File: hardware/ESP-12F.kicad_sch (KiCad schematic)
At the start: 37 parts, among them J10 PROG_PORT, U10 ESP-12F, U11 MCP2558FD-xMF, U8 PI4IOE5V6416LEX, U9 PI4IOE5V6416LEX

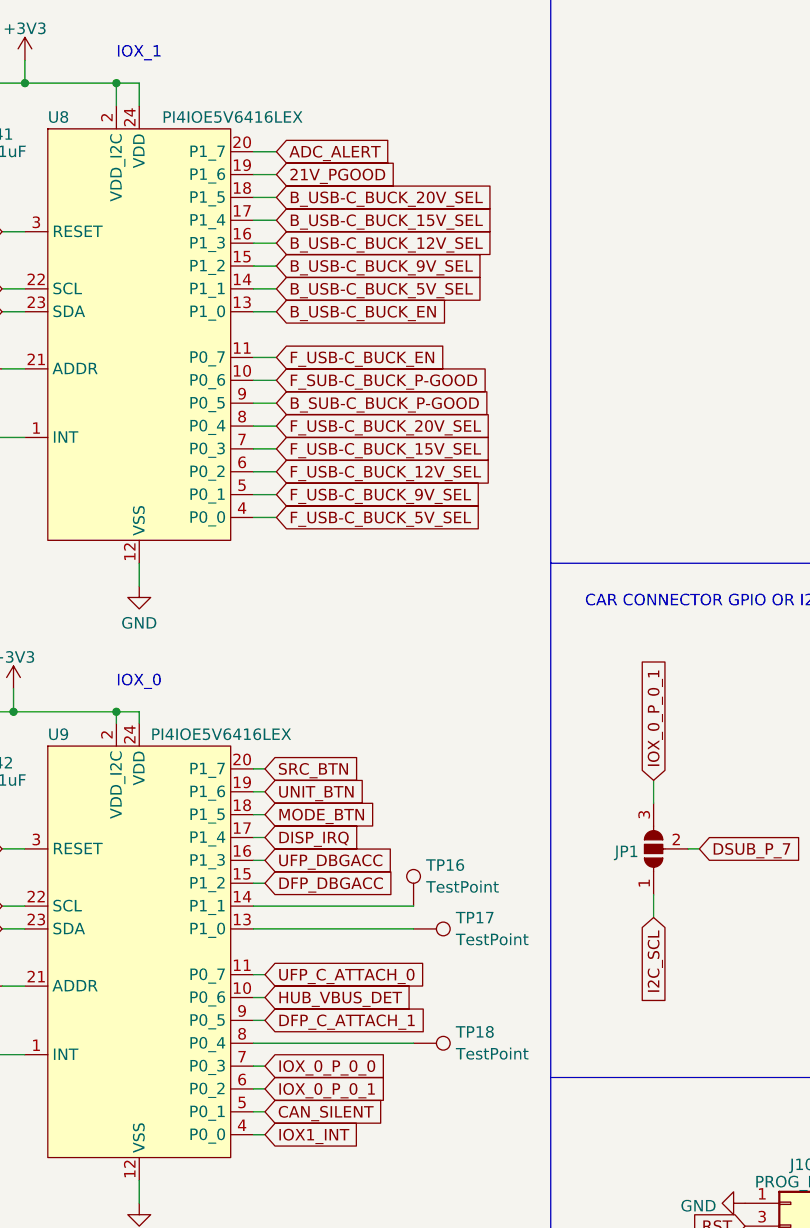
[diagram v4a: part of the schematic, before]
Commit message: switched pd phy as old one needed an NDA
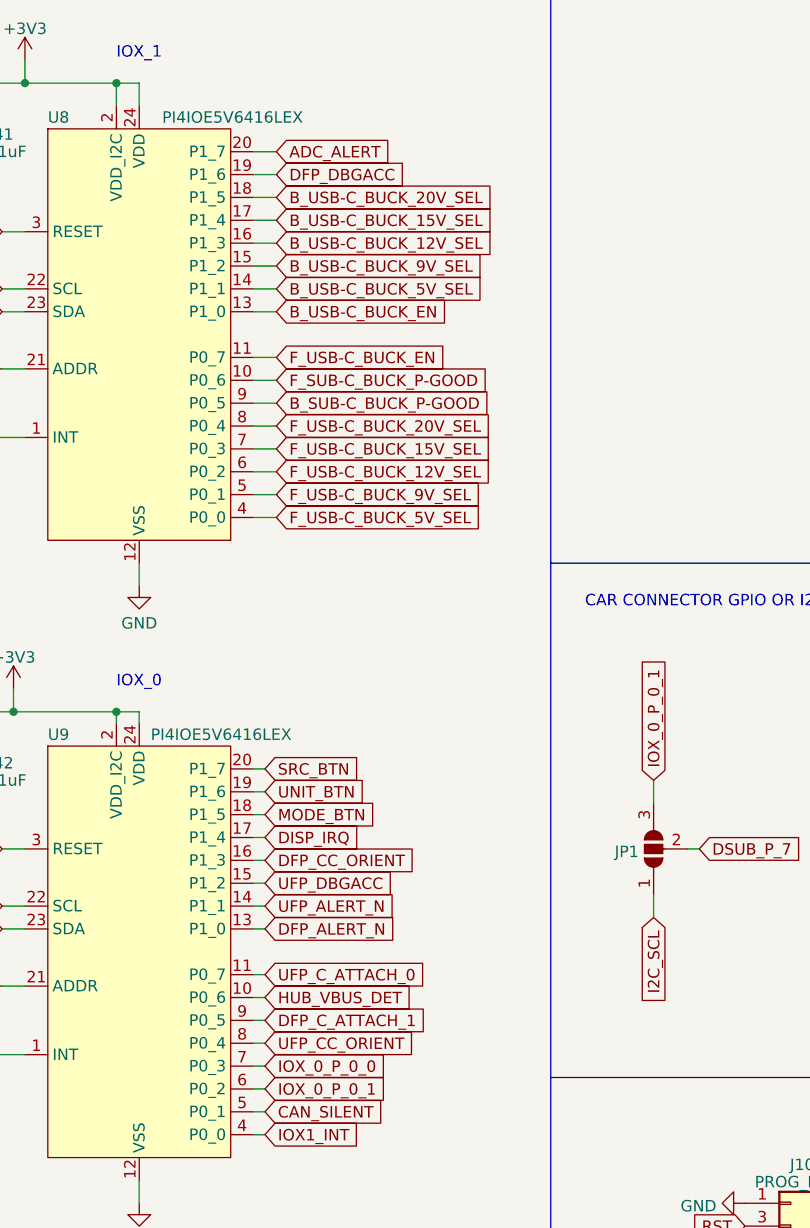
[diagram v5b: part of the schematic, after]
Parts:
- removed TP16, TP17, TP18: TestPoint, TestPoint:TestPoint_Pad_D1.5mm, symbol Connector:TestPoint
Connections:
- net 21V_PGOOD is gone; now on net DFP_DBGACC: U8.19 (P1_6)
- net DFP_DBGACC: no longer U9.15 (P1_2)
- net UFP_DBGACC: now also U9.15 (P1_2); no longer U9.16 (P1_3)
- net DFP_ALERT_N: now reaches U9.13 (P1_0)
- net UFP_ALERT_N: now reaches U9.14 (P1_1)
- net UFP_CC_ORIENT: now reaches U9.8 (P0_4)
- new net DFP_CC_ORIENT: U9.16 (P1_3)
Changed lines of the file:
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@@
-    (stroke (width 0) (type default))
-  )
-  (wire (pts (xy 82.55 149.86) (xy 100.33 149.86))
     (stroke (width 0) (type default))
   )
@@
     (stroke (width 0) (type default))
   )
+  (wire (pts (xy 82.55 149.86) (xy 83.82 149.86))
+    (stroke (width 0) (type default))
+  )
   (wire (pts (xy 217.17 130.81) (xy 219.71 130.81))
     (stroke (width 0) (type default))
@@
     (stroke (width 0) (type default))
   )
-  (wire (pts (xy 82.55 137.16) (xy 100.33 137.16))
-    (stroke (width 0) (type default))
-  )
   (wire (pts (xy 82.55 124.46) (xy 83.82 124.46))
     (stroke (width 0) (type default))
@@
     (stroke (width 0) (type default))
   )
+  (wire (pts (xy 82.55 137.16) (xy 83.82 137.16))
+    (stroke (width 0) (type default))
+  )
   (wire (pts (xy 153.67 133.35) (xy 153.67 135.89))
     (stroke (width 0) (type default))
@@
     (stroke (width 0) (type default))
   )
+  (wire (pts (xy 82.55 134.62) (xy 83.82 134.62))
+    (stroke (width 0) (type default))
+  )
   (wire (pts (xy 49.53 43.18) (xy 49.53 45.72))
     (stroke (width 0) (type default))
@@
   )
   (wire (pts (xy 201.93 87.63) (xy 201.93 83.82))
-    (stroke (width 0) (type default))
-  )
-  (wire (pts (xy 82.55 134.62) (xy 100.33 134.62))
     (stroke (width 0) (type default))
   )
@@
     )
   )
+  (global_label "UFP_CC_ORIENT" (shape input) (at 83.82 149.86 0) (fields_autoplaced)
+    (effects (font (size 1.27 1.27)) (justify left))
+    (property "Intersheetrefs" "${INTERSHEET_REFS}" (at 101.6219 149.86 0)
+      (effects (font (size 1.27 1.27)) (justify left) hide)
+    )
+  )
   (global_label "F_USB-C_BUCK_5V_SEL" (shape input) (at 85.09 91.44 0) (fields_autoplaced)
     (effects (font (size 1.27 1.27)) (justify left))
@@
     (effects (font (size 1.27 1.27)) (justify left))
     (property "Intersheetrefs" "${INTERSHEET_REFS}" (at 111.8233 81.28 0)
-      (effects (font (size 1.27 1.27)) (justify left) hide)
-    )
-  )
-  (global_label "21V_PGOOD" (shape input) (at 85.09 53.34 0) (fields_autoplaced)
-    (effects (font (size 1.27 1.27)) (justify left))
-    (property "Intersheetrefs" "${INTERSHEET_REFS}" (at 98.942 53.34 0)
       (effects (font (size 1.27 1.27)) (justify left) hide)
     )
@@
     )
   )
+  (global_label "UFP_ALERT_N" (shape input) (at 83.82 134.62 0) (fields_autoplaced)
+    (effects (font (size 1.27 1.27)) (justify left))
+    (property "Intersheetrefs" "${INTERSHEET_REFS}" (at 99.2633 134.62 0)
+      (effects (font (size 1.27 1.27)) (justify left) hide)
+    )
+  )
   (global_label "I2C_SDA" (shape input) (at 261.62 60.96 90) (fields_autoplaced)
     (effects (font (size 1.27 1.27)) (justify left))
@@
     )
   )
-  (global_label "UFP_DBGACC" (shape input) (at 83.82 129.54 0) (fields_autoplaced)
-    (effects (font (size 1.27 1.27)) (justify left))
-    (property "Intersheetrefs" "${INTERSHEET_REFS}" (at 98.8211 129.54 0)
+  (global_label "DFP_ALERT_N" (shape input) (at 83.82 137.16 0) (fields_autoplaced)
+    (effects (font (size 1.27 1.27)) (justify left))
+    (property "Intersheetrefs" "${INTERSHEET_REFS}" (at 99.2028 137.16 0)
+      (effects (font (size 1.27 1.27)) (justify left) hide)
+    )
+  )
+  (global_label "UFP_DBGACC" (shape input) (at 83.82 132.08 0) (fields_autoplaced)
+    (effects (font (size 1.27 1.27)) (justify left))
+    (property "Intersheetrefs" "${INTERSHEET_REFS}" (at 98.8211 132.08 0)
       (effects (font (size 1.27 1.27)) (justify left) hide)
     )
@@
     )
   )
-  (global_label "DFP_DBGACC" (shape input) (at 83.82 132.08 0) (fields_autoplaced)
-    (effects (font (size 1.27 1.27)) (justify left))
-    (property "Intersheetrefs" "${INTERSHEET_REFS}" (at 98.7606 132.08 0)
+  (global_label "DFP_DBGACC" (shape input) (at 85.09 53.34 0) (fields_autoplaced)
+    (effects (font (size 1.27 1.27)) (justify left))
+    (property "Intersheetrefs" "${INTERSHEET_REFS}" (at 100.0306 53.34 0)
       (effects (font (size 1.27 1.27)) (justify left) hide)
     )
@@
     (effects (font (size 1.27 1.27)) (justify left))
     (property "Intersheetrefs" "${INTERSHEET_REFS}" (at 106.441 73.66 0)
+      (effects (font (size 1.27 1.27)) (justify left) hide)
+    )
+  )
+  (global_label "DFP_CC_ORIENT" (shape input) (at 83.82 129.54 0) (fields_autoplaced)
+    (effects (font (size 1.27 1.27)) (justify left))
+    (property "Intersheetrefs" "${INTERSHEET_REFS}" (at 101.5614 129.54 0)
       (effects (font (size 1.27 1.27)) (justify left) hide)
     )
@@
         (path "/fae025e9-99c5-40c1-af6f-99dc1edbfa43/62352716-6578-44e5-ac45-fc6ae860b12d"
           (reference "#PWR049") (unit 1)
-        )
-      )
-    )
-  )
-  (symbol (lib_id "Connector:TestPoint") (at 100.33 137.16 270) (unit 1)
-    (in_bom yes) (on_board yes) (dnp no) (fields_autoplaced)
-    (property "Reference" "TP17" (at 105.029 135.9479 90)
-      (effects (font (size 1.27 1.27)) (justify left))
-    )
-    (property "Value" "TestPoint" (at 105.029 138.3721 90)
-      (effects (font (size 1.27 1.27)) (justify left))
-    )
-    (property "Footprint" "TestPoint:TestPoint_Pad_D1.5mm" (at 100.33 142.24 0)
-      (effects (font (size 1.27 1.27)) hide)
-    )
-    (property "Datasheet" "~" (at 100.33 142.24 0)
-      (effects (font (size 1.27 1.27)) hide)
-    )
-    (pin "1")
-    (instances
-      (project "usbc-car-module"
-        (path "/fae025e9-99c5-40c1-af6f-99dc1edbfa43/62352716-6578-44e5-ac45-fc6ae860b12d"
-          (reference "TP17") (unit 1)
         )
       )
@@
         )
       )
-    )
-  )
-  (symbol (lib_id "Connector:TestPoint") (at 100.33 149.86 270) (unit 1)
-    (in_bom yes) (on_board yes) (dnp no) (fields_autoplaced)
-    (property "Reference" "TP18" (at 105.029 148.6479 90)
-      (effects (font (size 1.27 1.27)) (justify left))
-    )
-    (property "Value" "TestPoint" (at 105.029 151.0721 90)
-      (effects (font (size 1.27 1.27)) (justify left))
-    )
-    (property "Footprint" "TestPoint:TestPoint_Pad_D1.5mm" (at 100.33 154.94 0)
-      (effects (font (size 1.27 1.27)) hide)
-    )
-    (property "Datasheet" "~" (at 100.33 154.94 0)
-      (effects (font (size 1.27 1.27)) hide)
-    )
-    (pin "1")
-    (instances
-      (project "usbc-car-module"
-        (path "/fae025e9-99c5-40c1-af6f-99dc1edbfa43/62352716-6578-44e5-ac45-fc6ae860b12d"
-          (reference "TP18") (unit 1)
-        )
-      )
-    )
-  )
-  (symbol (lib_id "Connector:TestPoint") (at 100.33 134.62 0) (unit 1)
-    (in_bom yes) (on_board yes) (dnp no) (fields_autoplaced)
-    (property "Reference" "TP16" (at 101.727 130.1059 0)
-      (effects (font (size 1.27 1.27)) (justify left))
-    )
-    (property "Value" "TestPoint" (at 101.727 132.5301 0)
-      (effects (font (size 1.27 1.27)) (justify left))
-    )
-    (property "Footprint" "TestPoint:TestPoint_Pad_D1.5mm" (at 105.41 134.62 0)
-      (effects (font (size 1.27 1.27)) hide)
-    )
-    (property "Datasheet" "~" (at 105.41 134.62 0)
-      (effects (font (size 1.27 1.27)) hide)
-    )
-    (pin "1")
-    (instances
-      (project "usbc-car-module"
-        (path "/fae025e9-99c5-40c1-af6f-99dc1edbfa43/62352716-6578-44e5-ac45-fc6ae860b12d"
-          (reference "TP16") (unit 1)
-        )
-      )

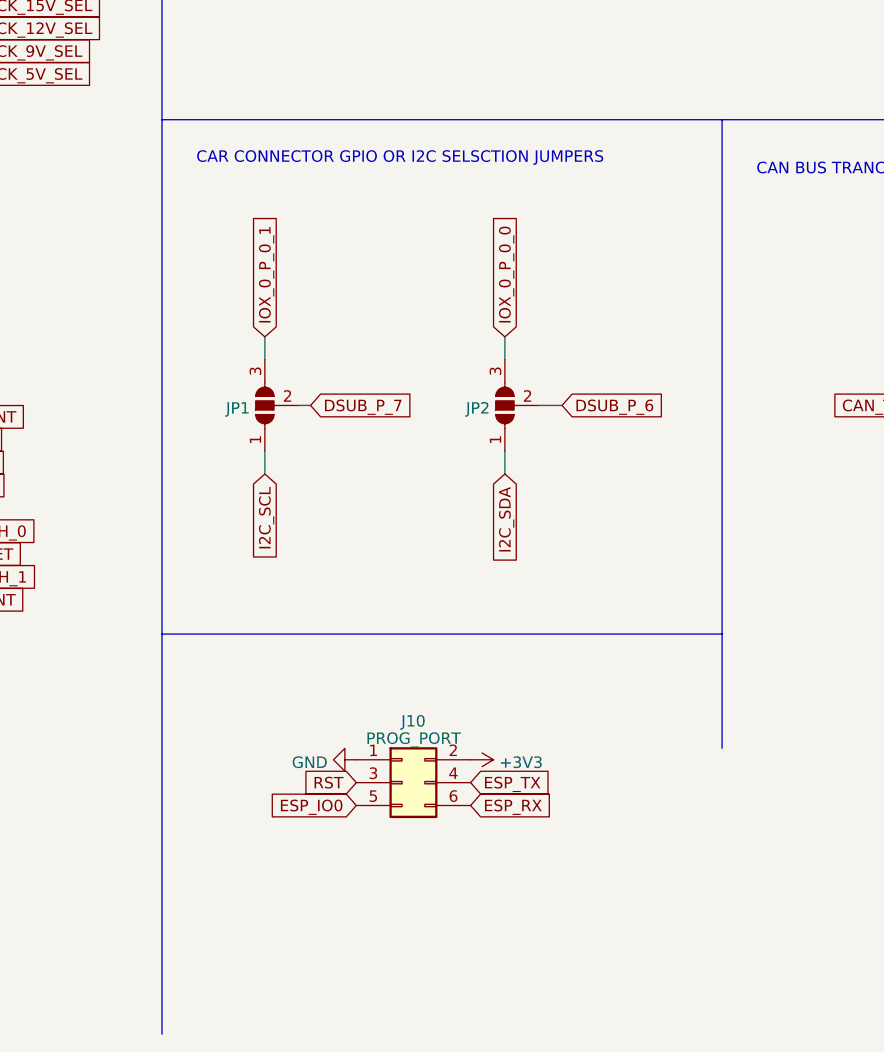
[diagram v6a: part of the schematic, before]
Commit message: added eeprom for nonvol memory
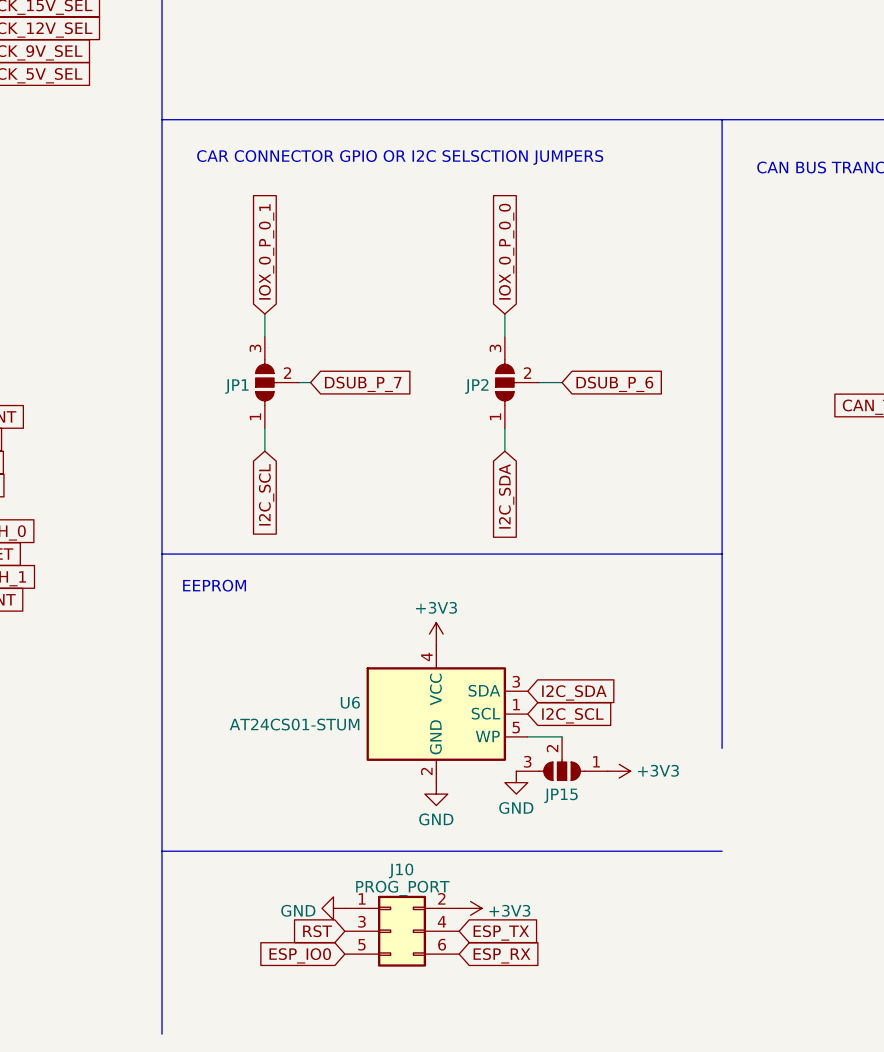
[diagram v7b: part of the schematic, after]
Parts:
- added JP15: ~, Jumper:SolderJumper-3_P1.3mm_Open_RoundedPad1.0x1.5mm_NumberLabels, symbol Jumper:SolderJumper_3_Open
- added U6: AT24CS01-STUM, Package_TO_SOT_SMD:SOT-23-5, symbol Memory_EEPROM:AT24CS01-STUM
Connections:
- net +3V3: now also JP15.1 (A), U6.4 (VCC)
- net GND: now also JP15.3 (B), U6.2 (GND)
- net I2C_SCL: now also U6.1 (SCL)
- net I2C_SDA: now also U6.3 (SDA)
- new net: JP15.2 (C), U6.5 (WP)
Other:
- note added: "EEPROM"
- moved on the sheet: J10, JP1, JP2

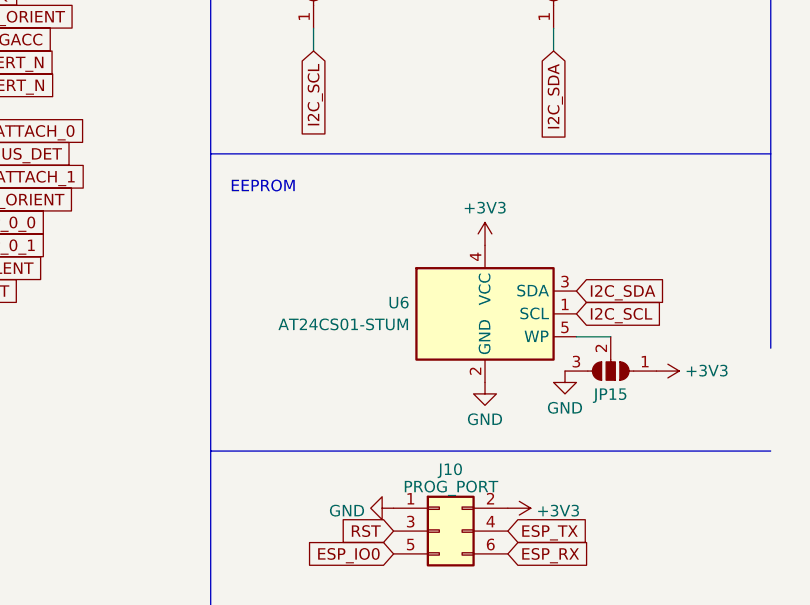
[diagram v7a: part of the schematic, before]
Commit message: fixed a shiton of spelling mistakes and some minor refactoring
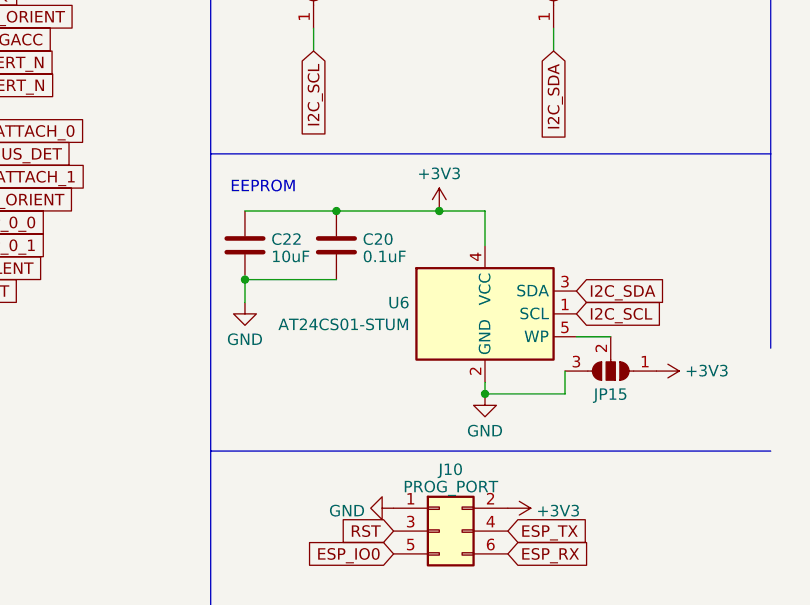
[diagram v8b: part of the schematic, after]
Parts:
- added C20: 0.1uF, Capacitor_SMD:C_0603_1608Metric, symbol Device:C
- added C22: 10uF, Capacitor_SMD:C_0603_1608Metric, symbol Device:C
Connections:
- net +3V3: now also C20.1, C22.1
- net GND: now also C20.2, C22.2
